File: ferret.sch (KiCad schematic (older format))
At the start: 59 parts, among them J1 USB_C_Receptacle, J2 Jack-DC, J3 BAT, Q1 40V, Q2 40V, Q3 40V, Q4 40V, U1 TPD6S300A, U2 FUSB307BMPX, U3 BQ25792, U4 TPS560430X3F

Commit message: almost done
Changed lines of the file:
@@
 Connection ~ 3150 3250
 $Sheet
-S 5100 6000 1250 1150
+S 5600 5200 700  800
 U 5EF44CB5
 F0 "MCU" 50
 F1 "MCU.sch" 50
+F2 "~INT_PMC" I L 5600 5350 50
+F3 "EN_SNK" I L 5600 5550 50
+F4 "~CE" O L 5600 5650 50
+F5 "SCL" O L 5600 5750 50
+F6 "SDA" B L 5600 5850 50
+F7 "~INT_CHG" I L 5600 5450 50
 $EndSheet
 Text Notes 750  6200 0    50   ~ 0
@@
 Text Label 3800 6750 2    50   ~ 0
 ~PROT_FLT
+Text Label 5200 5650 0    50   ~ 0
+~CE
+Text Label 5200 5850 0    50   ~ 0
+SDA
+Text Label 5200 5750 0    50   ~ 0
+SCL
+Text Label 5200 5450 0    50   ~ 0
+~INT_CHG
+Text Label 5200 5350 0    50   ~ 0
+~INT_PMC
+Text Label 5200 5550 0    50   ~ 0
+EN_SNK
+Wire Wire Line
+	5200 5350 5600 5350
+Wire Wire Line
+	5600 5450 5200 5450
+Wire Wire Line
+	5200 5550 5600 5550
+Wire Wire Line
+	5600 5650 5200 5650
+Wire Wire Line
+	5600 5750 5200 5750
+Wire Wire Line
+	5200 5850 5600 5850
 $EndSCHEMATC

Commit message: Looks good, just needs some more checking
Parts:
- added J3: GND/RS485 L, Connector_PinHeader_2.54mm:PinHeader_2x04_P2.54mm_Horizontal, symbol Connector_Generic:Conn_02x04_Odd_Even
- added J4: BAT+ L, Connector_PinHeader_2.54mm:PinHeader_2x04_P2.54mm_Horizontal, symbol Connector_Generic:Conn_02x04_Odd_Even
- added J5: GND/RS485 R, Connector_PinHeader_2.54mm:PinHeader_2x04_P2.54mm_Horizontal, symbol Connector_Generic:Conn_02x04_Odd_Even
- added J6: BAT+ R, Connector_PinHeader_2.54mm:PinHeader_2x04_P2.54mm_Horizontal, symbol Connector_Generic:Conn_02x04_Odd_Even
- added J8: Jack-DC, Connector_BarrelJack:BarrelJack_Horizontal, symbol Connector:Jack-DC
- added TP1: VBUS_USB, TestPoint:TestPoint_THTPad_D2.0mm_Drill1.0mm, symbol Connector:TestPoint_Small
- added TP2: ACDRV1, TestPoint:TestPoint_THTPad_D2.0mm_Drill1.0mm, symbol Connector:TestPoint_Small
- added TP3: VBUS_DC, TestPoint:TestPoint_THTPad_D2.0mm_Drill1.0mm, symbol Connector:TestPoint_Small
- added TP4: ACDRV2, TestPoint:TestPoint_THTPad_D2.0mm_Drill1.0mm, symbol Connector:TestPoint_Small
- added TP5: VBUS, TestPoint:TestPoint_THTPad_D2.0mm_Drill1.0mm, symbol Connector:TestPoint_Small
- added TP6: VCC, TestPoint:TestPoint_THTPad_D2.0mm_Drill1.0mm, symbol Connector:TestPoint_Small
- added TP7: +3V3, TestPoint:TestPoint_THTPad_D2.0mm_Drill1.0mm, symbol Connector:TestPoint_Small
- J2: footprint (none) -> Connector_BarrelJack:BarrelJack_Horizontal
- renumbered C2 to C1, C15 to C14, C14 to C15, C17 to C16, C18 to C17, C19 to C18, C20 to C19, C1 to C2, C21 to C20, C23 to C21, C24 to C22, C25 to C23, C16 to C24, C26 to C25, C27 to C26, C28 to C27, C29 to C28, C22 to C29, C7 to C6, C6 to C7, D2 to D1, D1 to D2, J3 to J7, R2 to R1, R13 to R11, R11 to R12, R12 to R13, R3 to R2, R4 to R3, R1 to R4, U2 to U1, U1 to U2
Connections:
- net +3V3: now also TP7.1
- net ACDRV1: now also TP2.1
- net ACDRV2: now also TP4.1
- net GND: now also J3.3 (Pin_3), J3.4 (Pin_4), J3.5 (Pin_5), J3.6 (Pin_6), J3.7 (Pin_7), J3.8 (Pin_8), J5.3 (Pin_3), J5.4 (Pin_4), J5.5 (Pin_5), J5.6 (Pin_6), J5.7 (Pin_7), J5.8 (Pin_8), J8.2
- net VAC1: now also TP1.1
- net VAC2: now also TP3.1
- net VBAT: now also J4.1 (Pin_1), J4.2 (Pin_2), J4.3 (Pin_3), J4.4 (Pin_4), J4.5 (Pin_5), J4.6 (Pin_6), J4.7 (Pin_7), J4.8 (Pin_8), J6.1 (Pin_1), J6.2 (Pin_2), J6.3 (Pin_3), J6.4 (Pin_4), J6.5 (Pin_5), J6.6 (Pin_6), J6.7 (Pin_7), J6.8 (Pin_8), J8.1
- net VBUS: now also TP5.1
- net VCC: now also TP6.1
- new net A: J3.1 (Pin_1), J5.1 (Pin_1)
- new net B: J3.2 (Pin_2), J5.2 (Pin_2)
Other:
- note added: "Power from Battery\nor external PSU"
- moved on the sheet: C1, C24, C3, C4, C5, C7, D1, L2, R1, R12, R13, R2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

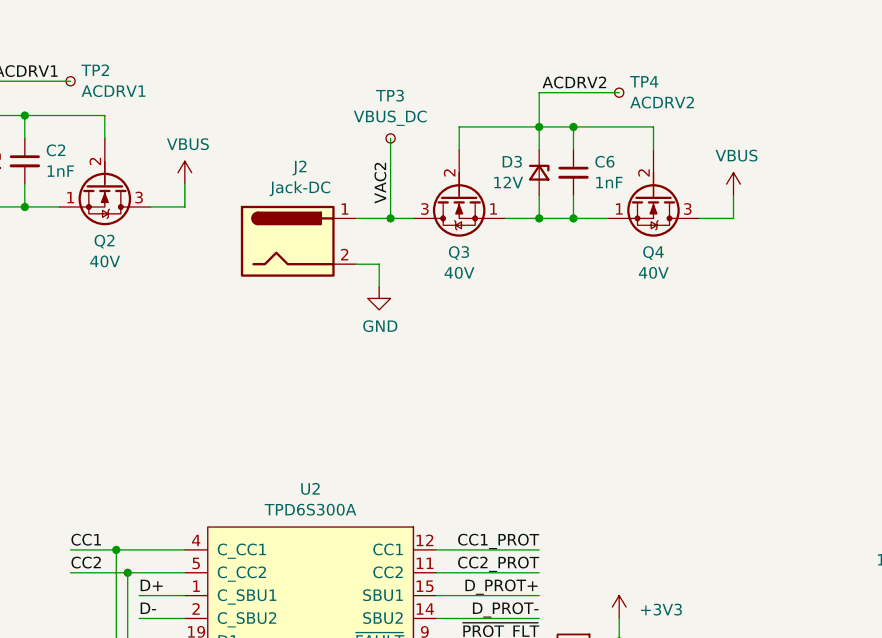
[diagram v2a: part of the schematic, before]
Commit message: added reverse polarity protection at VIN2
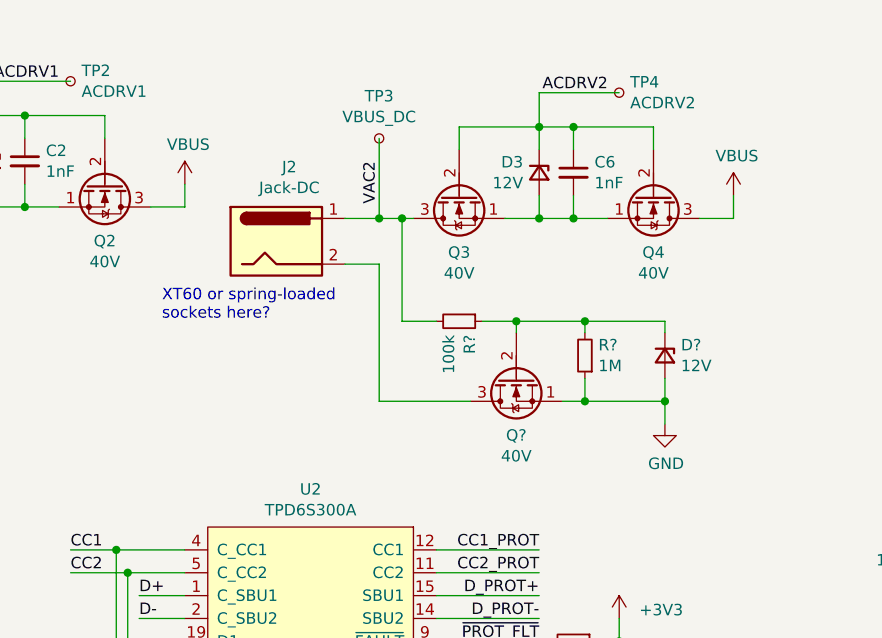
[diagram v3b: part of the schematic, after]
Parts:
- added D?: 12V, symbol Device:D_Zener_Small
- added Q?: 40V, symbol Device:Q_NMOS_SGD
- added R?: 1M, Resistor_SMD:R_0603_1608Metric, symbol Device:R_Small
- added R?: 100k, Resistor_SMD:R_0603_1608Metric, symbol Device:R_Small
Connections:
- net GND: now also D?.2 (A), Q?.1 (S), R?.1; no longer J2.2
- net VAC2: now also R?.2
- new net: J2.2, Q?.3 (D)
- new net: D?.1 (K), Q?.2 (G), R?.1, R?.2
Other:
- note added: "XT60 or spring-loaded\nsockets here?"
- moved on the sheet: J2, TP3
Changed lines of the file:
@@
 L Connector:Jack-DC J2
 U 1 1 5EEE8F90
-P 3900 1750
-F 0 "J2" H 3957 2075 50  0000 C CNN
-F 1 "Jack-DC" H 3957 1984 50  0000 C CNN
-F 2 "Connector_BarrelJack:BarrelJack_Horizontal" H 3950 1710 50  0001 C CNN
-F 3 "~" H 3950 1710 50  0001 C CNN
-	1    3900 1750
+P 3850 1750
+F 0 "J2" H 3907 2075 50  0000 C CNN
+F 1 "Jack-DC" H 3907 1984 50  0000 C CNN
+F 2 "Connector_BarrelJack:BarrelJack_Horizontal" H 3900 1710 50  0001 C CNN
+F 3 "~" H 3900 1710 50  0001 C CNN
+	1    3850 1750
 	1    0    0    -1
 $EndComp
@@
 L power:GND #PWR014
 U 1 1 5EEEAF6A
-P 4300 1950
-F 0 "#PWR014" H 4300 1700 50  0001 C CNN
-F 1 "GND" H 4305 1777 50  0000 C CNN
-F 2 "" H 4300 1950 50  0001 C CNN
-F 3 "" H 4300 1950 50  0001 C CNN
-	1    4300 1950
-	1    0    0    -1
-$EndComp
-Wire Wire Line
-	4300 1950 4300 1850
-Wire Wire Line
-	4300 1850 4200 1850
+P 5550 2550
+F 0 "#PWR014" H 5550 2300 50  0001 C CNN
+F 1 "GND" H 5555 2377 50  0000 C CNN
+F 2 "" H 5550 2550 50  0001 C CNN
+F 3 "" H 5550 2550 50  0001 C CNN
+	1    5550 2550
+	1    0    0    -1
+$EndComp
+Wire Wire Line
+	5550 2550 5550 2450
+Wire Wire Line
+	5550 2450 5200 2450
 NoConn ~ 1850 2600
 NoConn ~ 1850 2700
@@
 ACDRV2
 Wire Wire Line
-	4200 1650 4350 1650
+	4150 1650 4300 1650
 Wire Wire Line
 	5700 1650 5850 1650
@@
 Wire Wire Line
 	5850 1550 5850 1650
-Connection ~ 4350 1650
-Wire Wire Line
-	4350 1650 4450 1650
-Text Label 4350 1400 3    50   ~ 0
+Connection ~ 4300 1650
+Wire Wire Line
+	4300 1650 4400 1650
+Text Label 4300 1400 3    50   ~ 0
 VAC2
 Text Label 7950 1700 3    50   ~ 0
@@
 L Connector:TestPoint_Small TP3
 U 1 1 5F25CC29
-P 4350 1300
-F 0 "TP3" H 4350 1485 50  0000 C CNN
-F 1 "VBUS_DC" H 4350 1394 50  0000 C CNN
-F 2 "TestPoint:TestPoint_THTPad_D2.0mm_Drill1.0mm" H 4550 1300 50  0001 C CNN
-F 3 "~" H 4550 1300 50  0001 C CNN
-	1    4350 1300
-	1    0    0    -1
-$EndComp
-Wire Wire Line
-	4350 1300 4350 1650
+P 4300 1300
+F 0 "TP3" H 4300 1485 50  0000 C CNN
+F 1 "VBUS_DC" H 4300 1394 50  0000 C CNN
+F 2 "TestPoint:TestPoint_THTPad_D2.0mm_Drill1.0mm" H 4500 1300 50  0001 C CNN
+F 3 "~" H 4500 1300 50  0001 C CNN
+	1    4300 1300
+	1    0    0    -1
+$EndComp
+Wire Wire Line
+	4300 1300 4300 1650
 $Comp
 L Connector:TestPoint_Small TP5
@@
 Text Notes 10300 1250 0    50   ~ 0
 Power from Battery\nor external PSU
+$Comp
+L Device:Q_NMOS_SGD Q?
+U 1 1 5EF486C4
+P 4900 2350
+F 0 "Q?" V 5149 2350 50  0000 C CNN
+F 1 "40V" V 5240 2350 50  0000 C CNN
+F 2 "" H 5100 2450 50  0001 C CNN
+F 3 "~" H 4900 2350 50  0001 C CNN
+F 4 "SiSS10ADN" V 4900 2350 50  0001 C CNN "MPN"
+	1    4900 2350
+	0    -1   1    0
+$EndComp
+Wire Wire Line
+	4150 1850 4300 1850
+Wire Wire Line
+	4300 1850 4300 2450
+Wire Wire Line
+	4300 2450 4700 2450
+Text Notes 3350 2100 0    50   ~ 0
+XT60 or spring-loaded\nsockets here?
+$Comp
+L Device:D_Zener_Small D?
+U 1 1 5EF931C4
+P 5550 2250
+F 0 "D?" V 5504 2320 50  0000 L CNN
+F 1 "12V" V 5595 2320 50  0000 L CNN
+F 2 "" V 5550 2250 50  0001 C CNN
+F 3 "~" V 5550 2250 50  0001 C CNN
+	1    5550 2250
+	0    1    1    0
+$EndComp
+$Comp
+L Device:R_Small R?
+U 1 1 5EF93EA3
+P 5200 2250
+F 0 "R?" H 5141 2204 50  0000 R CNN
+F 1 "1M" H 5141 2295 50  0000 R CNN
+F 2 "Resistor_SMD:R_0603_1608Metric" H 5200 2250 50  0001 C CNN
+F 3 "~" H 5200 2250 50  0001 C CNN
+	1    5200 2250
+	-1   0    0    1
+$EndComp
+Wire Wire Line
+	5200 2350 5200 2450
+Connection ~ 5200 2450
+Wire Wire Line
+	5200 2450 5100 2450
+Wire Wire Line
+	5550 2350 5550 2450
+Connection ~ 5550 2450
+Wire Wire Line
+	5550 2150 5550 2100
+Wire Wire Line
+	5550 2100 5200 2100
+Wire Wire Line
+	4900 2100 4900 2150
+Wire Wire Line
+	5200 2150 5200 2100
+Connection ~ 5200 2100
+Wire Wire Line
+	5200 2100 4900 2100
+$Comp
+L Device:R_Small R?
+U 1 1 5F095217
+P 4650 2100
+F 0 "R?" H 4709 2146 50  0000 L CNN
+F 1 "100k" H 4709 2055 50  0000 L CNN
+F 2 "Resistor_SMD:R_0603_1608Metric" H 4650 2100 50  0001 C CNN
+F 3 "~" H 4650 2100 50  0001 C CNN
+	1    4650 2100
+	0    1    1    0
+$EndComp
+Wire Wire Line
+	4750 2100 4900 2100
+Connection ~ 4900 2100
+Wire Wire Line
+	4550 2100 4400 2100
+Wire Wire Line
+	4400 2100 4400 1650
+Connection ~ 4400 1650
+Wire Wire Line
+	4400 1650 4450 1650
 $EndSCHEMATC

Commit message: Add some footprints to parts
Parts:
- J1: footprint (none) -> Connector_USB:USB_C_Receptacle_XKB_U262-16XN-4BVC11; symbol Connector:USB_C_Receptacle -> Connector:USB_C_Receptacle_USB2.0
- L1: footprint (none) -> Inductor_SMD:L_Bourns_SRP1245A
- Q1, Q2, Q3, Q4: footprint (none) -> Package_SO:Vishay_PowerPAK_1212-8_Single
- Q5: renamed from Q?; footprint (none) -> Package_SO:Vishay_PowerPAK_1212-8_Single
- U3: footprint (none) -> Automated:Texas_VQFN-HR_RQM_4x4mm_P0.40-0.45mm
- gave numbers to parts that had none: 3
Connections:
- no-connect marks 13 -> 5
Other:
- moved on the sheet: C1, C2, C3, C4, C5, C6, C7, D1, D15, D2, D3, J2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

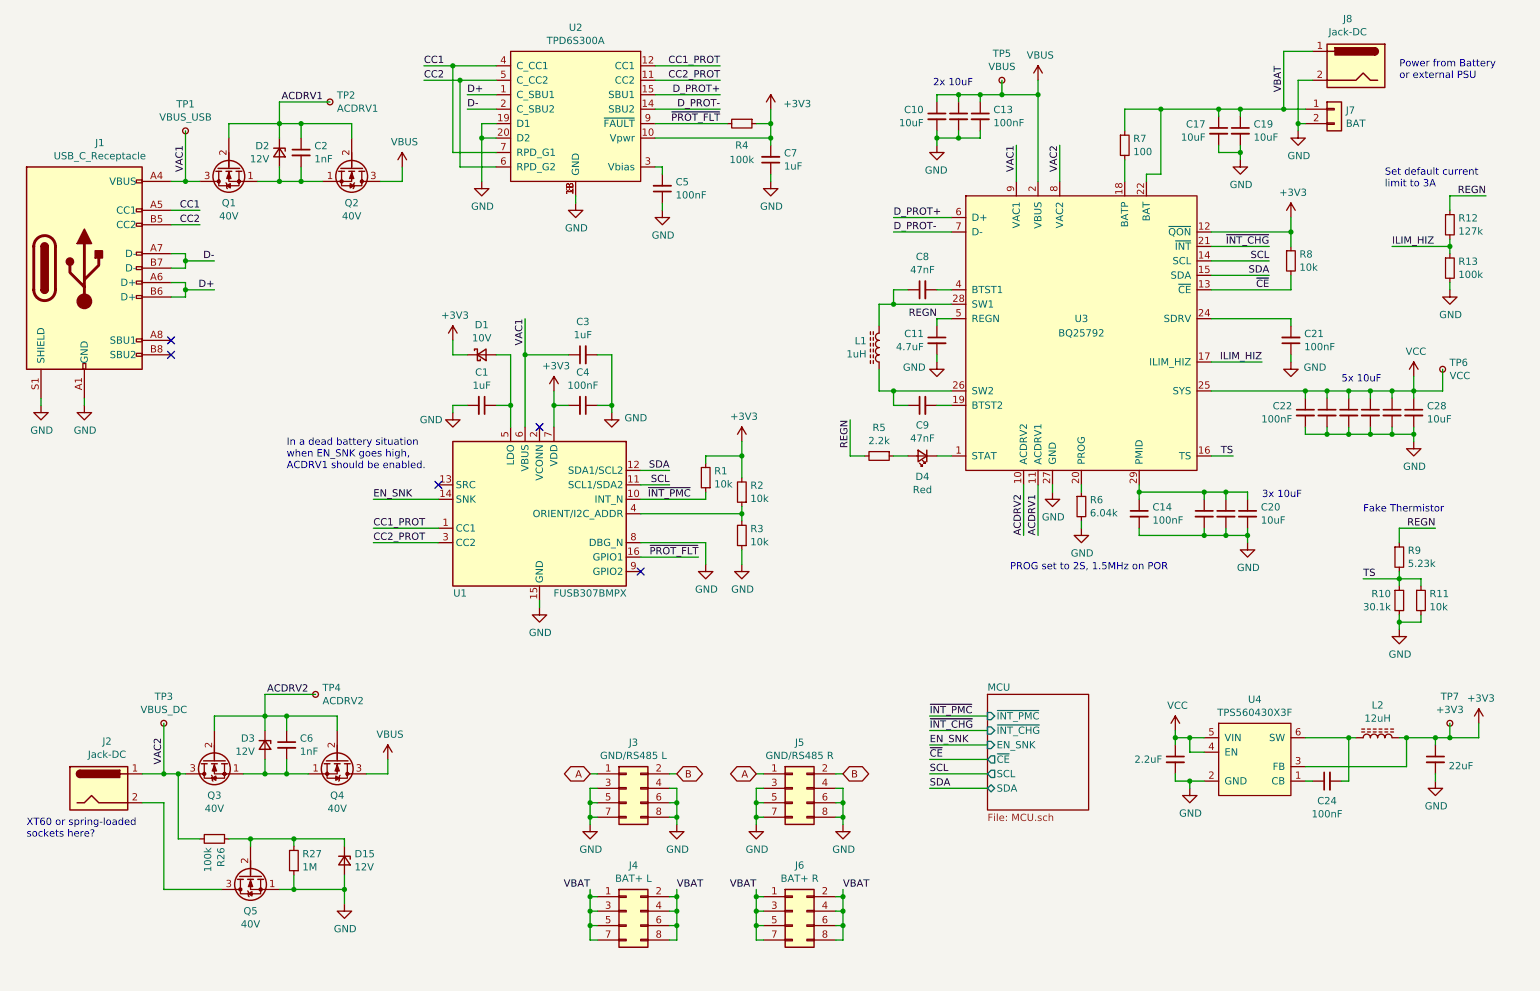
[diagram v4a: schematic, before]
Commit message: Re-annotated, add more footprints
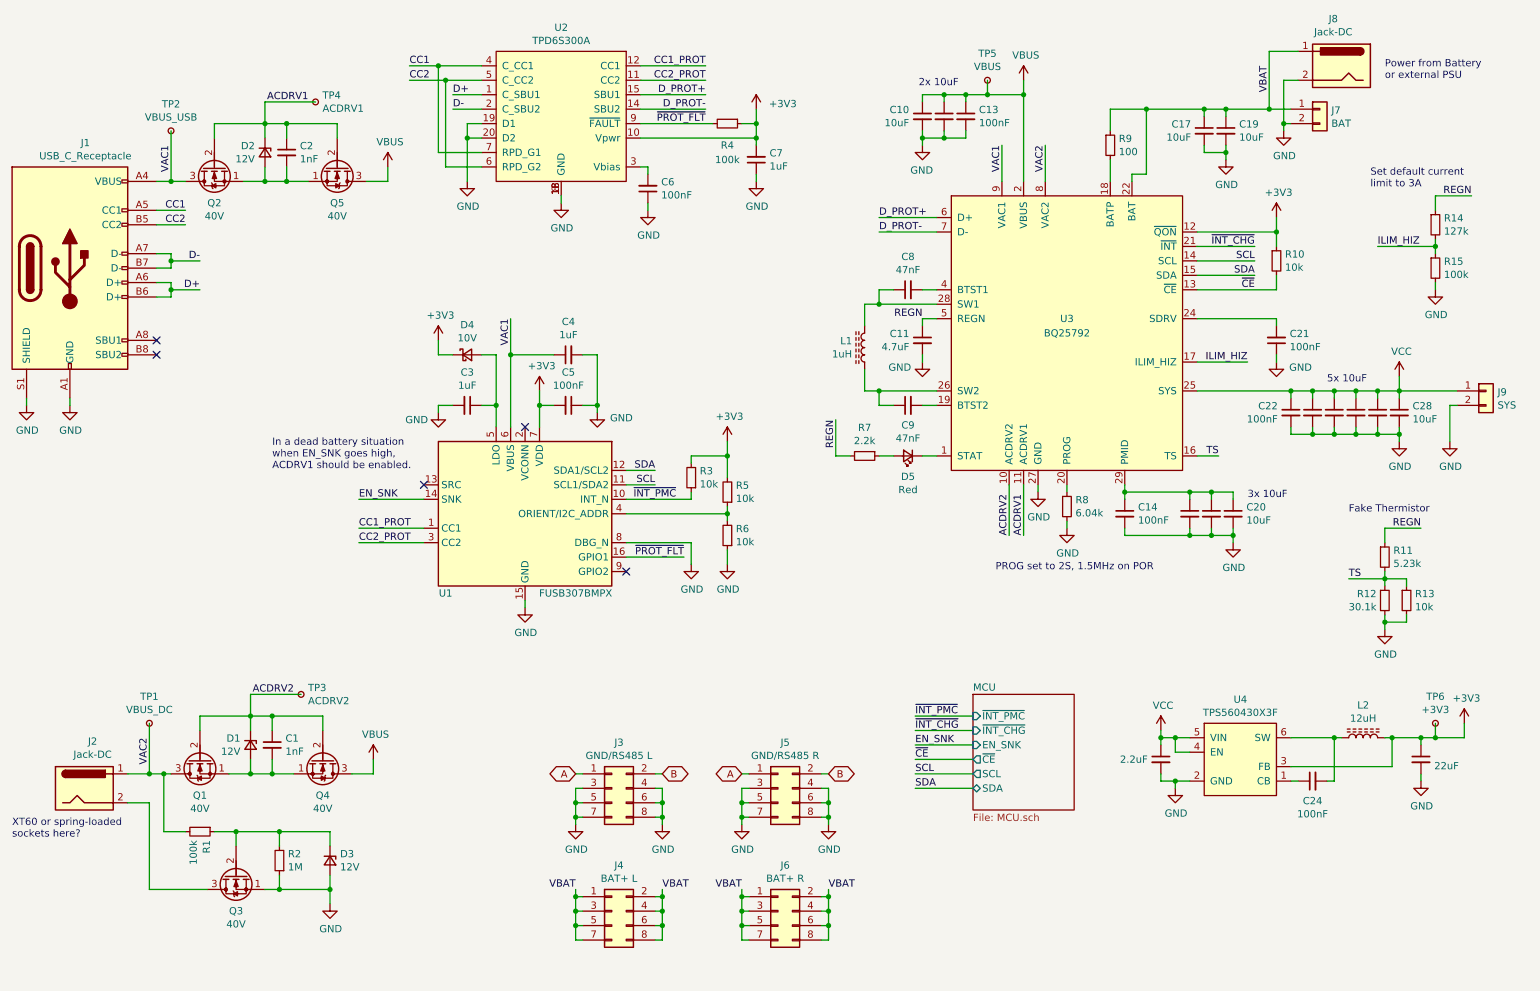
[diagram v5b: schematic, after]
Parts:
- removed TP6: VCC, TestPoint:TestPoint_THTPad_D2.0mm_Drill1.0mm, symbol Connector:TestPoint_Small
- added J9: SYS, Connector_PinSocket_2.54mm:PinSocket_1x02_P2.54mm_Vertical, symbol Connector_Generic:Conn_01x02
- D4: renamed from D1; footprint (none) -> Diode_SMD:D_SOD-123; MPN (none) -> BAT54W
- D5: renamed from D4; footprint (none) -> LED_SMD:LED_0603_1608Metric_Castellated
- renumbered C6 to C1, C1 to C3, C3 to C4, C4 to C5, C5 to C6, D3 to D1, D15 to D3, Q3 to Q1, Q1 to Q2, Q5 to Q3, Q2 to Q5, R26 to R1, R8 to R10, R9 to R11, R10 to R12, R11 to R13, R12 to R14, R13 to R15, R27 to R2, R1 to R3, R2 to R5, R3 to R6, R5 to R7, R6 to R8, R7 to R9, TP3 to TP1, TP1 to TP2, TP4 to TP3, TP2 to TP4, TP7 to TP6
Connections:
- net GND: now also J9.2 (Pin_2)
- net VCC: now also J9.1 (Pin_1)
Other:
- moved on the sheet: C1, C10, C11, C13, C14, C17, C19, C2, C20, C21, C22, C24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

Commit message: Some more work
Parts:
- D1, D2, D3: footprint (none) -> Diode_SMD:D_SOD-523
- J7: footprint (none) -> Automated:Conn_AMASS_XT60PW-F20
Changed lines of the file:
@@
 F 0 "J7" H 9830 1442 50  0000 L CNN
 F 1 "BAT" H 9830 1351 50  0000 L CNN
-F 2 "" H 9750 1450 50  0001 C CNN
+F 2 "Automated:Conn_AMASS_XT60PW-F20" H 9750 1450 50  0001 C CNN
 F 3 "~" H 9750 1450 50  0001 C CNN
 	1    9750 1450
@@
 F 0 "D2" V 2404 1680 50  0000 R CNN
 F 1 "12V" V 2495 1680 50  0000 R CNN
-F 2 "" V 2450 1750 50  0001 C CNN
+F 2 "Diode_SMD:D_SOD-523" V 2450 1750 50  0001 C CNN
 F 3 "~" V 2450 1750 50  0001 C CNN
 	1    2450 1750
@@
 F 1 "TPS560430X3F" H 9200 6274 50  0000 C CNN
 F 2 "Package_TO_SOT_SMD:SOT-23-6" H 9150 6250 50  0001 C CNN
-F 3 "" H 9000 6250 50  0001 C CNN
+F 3 "https://www.ti.com/lit/ds/symlink/tps560430.pdf" H 9000 6250 50  0001 C CNN
 	1    9200 5950
 	1    0    0    -1
@@
 F 0 "D1" V 2304 5780 50  0000 R CNN
 F 1 "12V" V 2395 5780 50  0000 R CNN
-F 2 "" V 2350 5850 50  0001 C CNN
+F 2 "Diode_SMD:D_SOD-523" V 2350 5850 50  0001 C CNN
 F 3 "~" V 2350 5850 50  0001 C CNN
 	1    2350 5850
@@
 F 0 "D3" V 2854 6720 50  0000 L CNN
 F 1 "12V" V 2945 6720 50  0000 L CNN
-F 2 "" V 2900 6650 50  0001 C CNN
+F 2 "Diode_SMD:D_SOD-523" V 2900 6650 50  0001 C CNN
 F 3 "~" V 2900 6650 50  0001 C CNN
 	1    2900 6650
